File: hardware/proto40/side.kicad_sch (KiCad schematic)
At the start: 18 parts, among them J1001 DIN41612_02x32_AC, U1001 TMUX1308, U1002 74HC595, U1003 74AHCT1G125

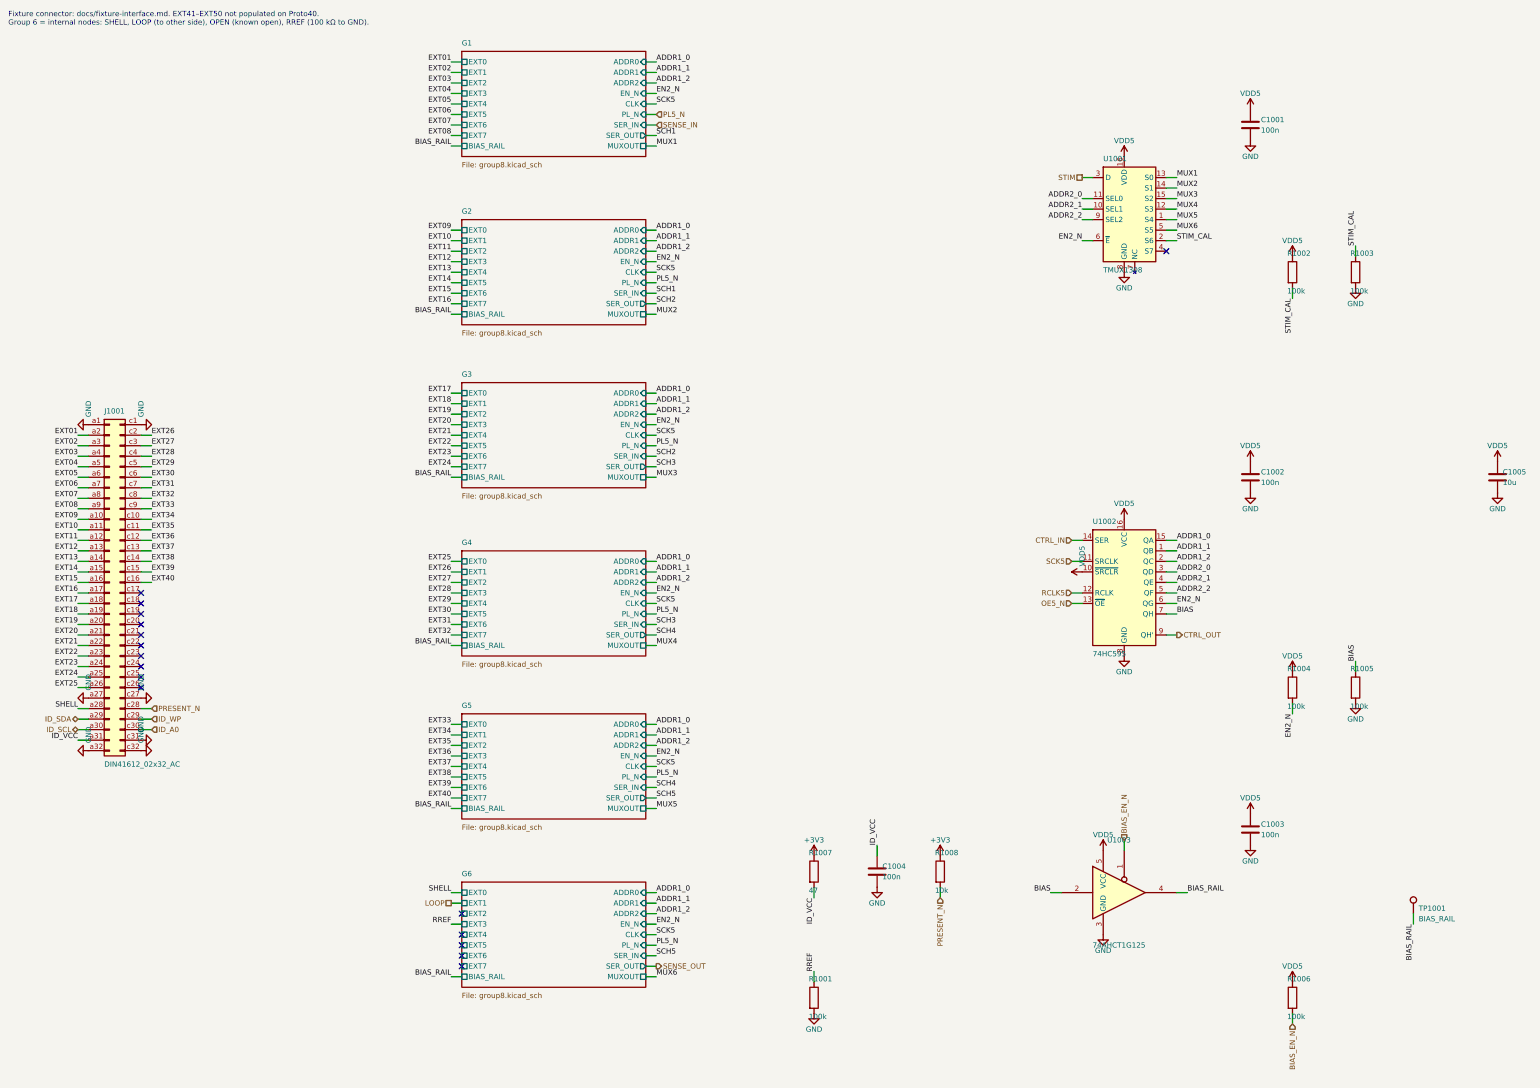
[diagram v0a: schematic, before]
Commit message: Redraw Proto40 schematic with wired functional blocks
Review feedback: text overlapped components and parts were isolated
islands joined only by labels, so connectivity was hard to follow.

- Generator: polyline wires, automatic junctions, text placement from
  the real symbol body graphics, KiCad field-angle handling for rotated
  symbols, power symbols oriented normally on horizontal pins
- Sheets redrawn left-to-right with wired blocks: channel cells, BIAS
  rail, decoupling on IC power pins, pull-ups on their lines, control
  ladder across the six groups, visible 165 chain, wired root hierarchy
  (MCU -> Control -> both sides) and cross-side LOOP
- layoutcheck.py: rejects text/text, text/body, text/wire overlaps and
  wires through bodies; CI runs the generator with --strict
- check_proto40.py: finds parts by sheet path and follows pins, so it no
  longer depends on net names or reference numbering

ERC 0 violations, design-intent audit PASS, layout issues 0.

Co-Authored-By: Claude Opus 5.5 <noreply@anthropic.com>
Claude-Session: https://claude.ai/code/session_01UG7pR5ZtgvoVGRWFojzQKf
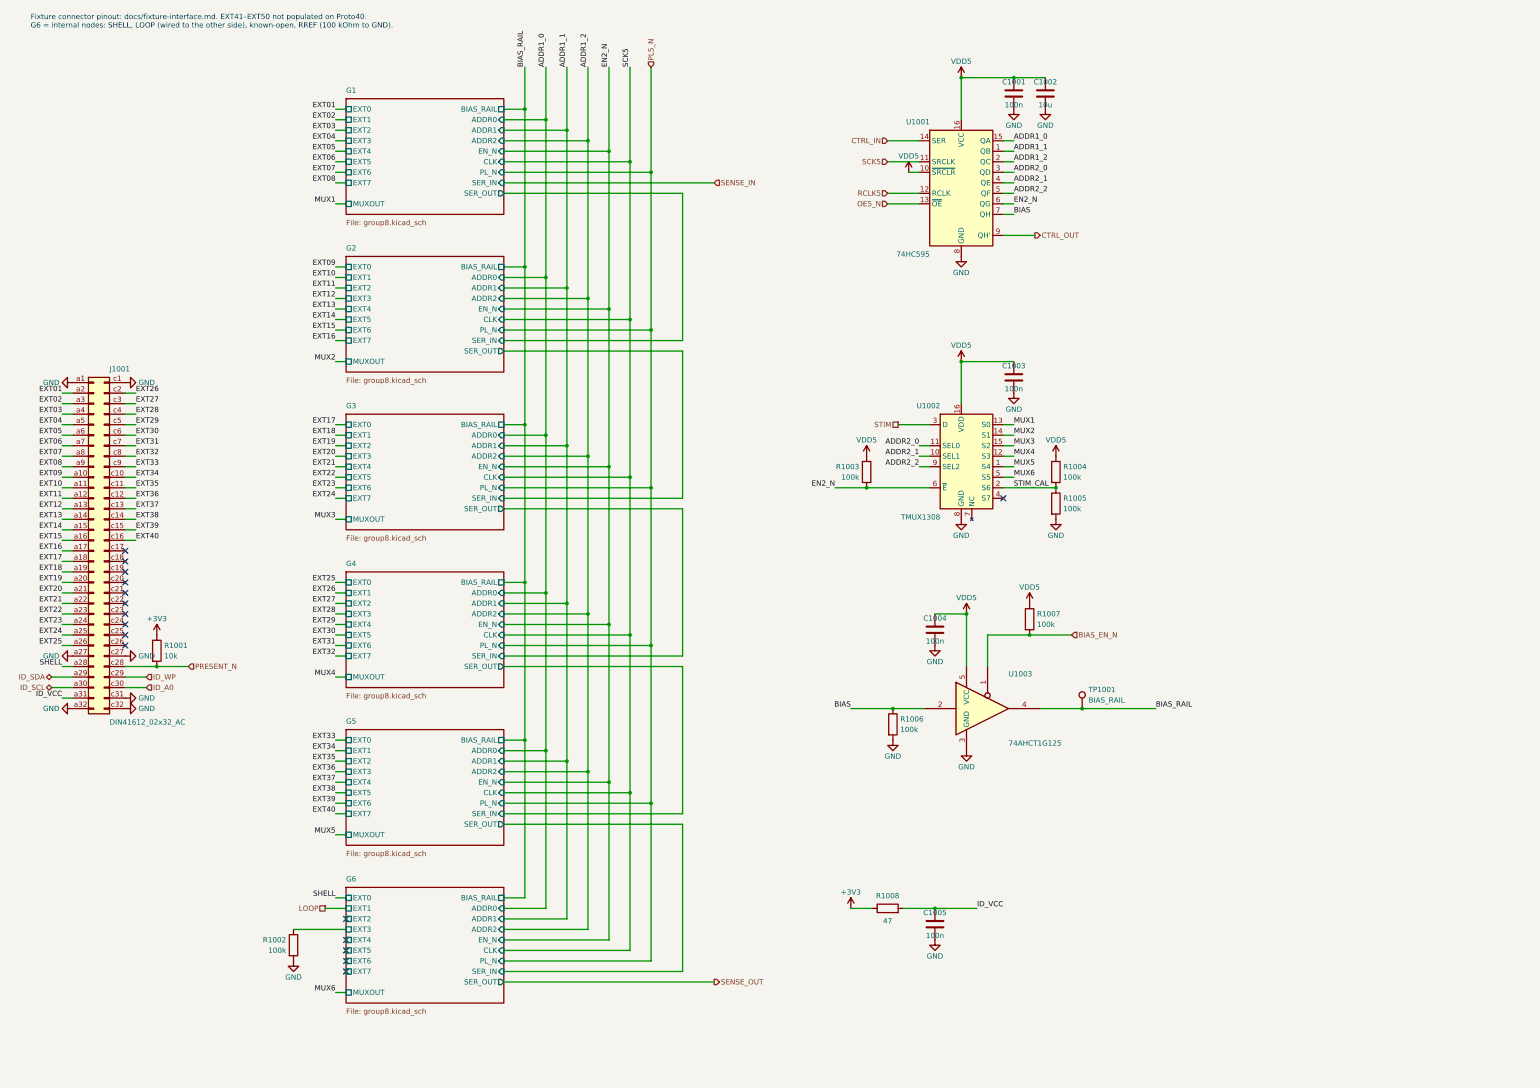
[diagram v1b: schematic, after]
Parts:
- C1002: value 100n -> 10u; footprint Capacitor_SMD:C_0603_1608Metric -> Capacitor_SMD:C_0805_2012Metric
- C1005: value 10u -> 100n; footprint Capacitor_SMD:C_0805_2012Metric -> Capacitor_SMD:C_0603_1608Metric
- R1001: value 100k -> 10k; Note load-signature reference node -> (none)
- R1002: Note (none) -> load-signature reference node
- R1003: Note (none) -> mux off while 595 outputs are Hi-Z
- R1004: Note mux disabled while 595 outputs are Hi-Z -> (none)
- R1005: Note bias low while 595 outputs are Hi-Z -> (none)
- R1006: Note bias Hi-Z until MCU enables -> bias low while 595 outputs are Hi-Z
- R1007: value 47 -> 100k; Note ID_VCC current limit -> bias Hi-Z until the MCU enables it
- R1008: value 10k -> 47; Note (none) -> ID_VCC current limit
- U1001: value TMUX1308 -> 74HC595; symbol cable_tester:TMUX1308 -> 74xx:74HC595; MPN (none) -> SN74HC595PWR; Manufacturer (none) -> Texas Instruments
- U1002: value 74HC595 -> TMUX1308; symbol 74xx:74HC595 -> cable_tester:TMUX1308; MPN SN74HC595PWR -> (none); Manufacturer Texas Instruments -> (none)
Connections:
- net RREF is gone; now on net +3V3: R1001.1
- net +3V3: no longer R1007.1
- net ADDR1_0: now also U1001.15 (QA); no longer U1002.15 (QA)
- net ADDR1_1: now also U1001.1 (QB); no longer U1002.1 (QB)
- net ADDR1_2: now also U1001.2 (QC); no longer U1002.2 (QC)
- net ADDR2_0: now also U1001.3 (QD), U1002.11 (SEL0); no longer U1001.11 (SEL0), U1002.3 (QD)
- net ADDR2_1: now also U1001.4 (QE), U1002.10 (SEL1); no longer U1001.10 (SEL1), U1002.4 (QE)
- net ADDR2_2: now also U1001.5 (QF), U1002.9 (SEL2); no longer U1001.9 (SEL2), U1002.5 (QF)
- net BIAS: now also R1006.1, U1001.7 (QH); no longer R1005.1, U1002.7 (QH)
- net BIAS_EN_N: now also R1007.2; no longer R1006.2
- net CTRL_IN: now also U1001.14 (SER); no longer U1002.14 (SER)
- net CTRL_OUT: now also U1001.9 (QH'); no longer U1002.9 (QH')
- net EN2_N: now also R1003.2; no longer R1004.2
- net GND: now also R1002.2, R1006.2; no longer R1001.2, R1003.2
- net ID_VCC: now also C1005.1, R1008.2; no longer C1004.1, R1007.2
- net MUX1: now also U1002.13 (S0); no longer U1001.13 (S0)
- net MUX2: now also U1002.14 (S1); no longer U1001.14 (S1)
- net MUX3: now also U1002.15 (S2); no longer U1001.15 (S2)
- net MUX4: now also U1002.12 (S3); no longer U1001.12 (S3)
- net MUX5: now also U1002.1 (S4); no longer U1001.1 (S4)
- net MUX6: now also U1002.5 (S5); no longer U1001.5 (S5)
- net OE5_N: now also U1001.13 (~{OE}); no longer U1002.13 (~{OE})
- net PRESENT_N: now also R1001.2; no longer R1008.2
- net RCLK5: now also U1001.12 (RCLK); no longer U1002.12 (RCLK)
- net SCK5: now also U1001.11 (SRCLK); no longer U1002.11 (SRCLK)
- net STIM: now also U1002.3 (D); no longer U1001.3 (D)
- net STIM_CAL: now also R1004.2, R1005.1, U1002.2 (S6); no longer R1002.2, R1003.1, U1001.2 (S6)
- net VDD5: now also C1004.1, R1003.1, R1007.1, U1001.10 (~{SRCLR}); no longer C1005.1, R1002.1, R1006.1, U1002.10 (~{SRCLR})
- new net G6/EXT3: R1002.1
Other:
- note added: "Fixture connector pinout: docs/fixture-interface.md. EXT41–EXT50 not populated on Proto40. G6 = internal nodes: SHELL, LOOP (wired to the other side), known-open, RREF (100 kOhm to GND)."
- note removed: "Fixture connector: docs/fixture-interface.md. EXT41–EXT50 not populated on Proto40. Group 6 = internal nodes: SHELL, LOOP (to other side), OPEN (known open), RREF (100 kΩ to GND)."
- moved on the sheet: C1001, C1002, C1003, C1004, C1005, J1001, R1001, R1002, R1003, R1004, R1005, R1006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
